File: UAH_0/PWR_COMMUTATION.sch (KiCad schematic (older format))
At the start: 19 parts

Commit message: обновлена схема управления движками
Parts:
- removed R1, R2, R6, R7: Резистор_10_кОм±5%_0,1Вт, MOTOR_RLC:Резистор_SMD_0603-0,075_Вт, symbol MOTOR_2020_import:Резистор_10_кОм±5%_0,1Вт
- removed R3, R4, R5: Резистор_470_Ом±5%_0,1Вт, MOTOR_RLC:Резистор_SMD_0603-0,075_Вт, symbol MOTOR_2020_import:Резистор_470_Ом±5%_0,1Вт
- removed VD3, VD5: Стабилитрон_2С133В, symbol MOTOR_2020_components:Стабилитрон_2С133В
- removed VT1, VT4: MOSFET_P-канал_IRF4905PBF, N_VD_HL:Транзистор_P_IRF9Z24NPBF, symbol elements_2020:MOSFET_P-канал_IRF4905PBF
- added C10, C11, C12, C13, C8, C9: Конденсатор_16В_0.1_мкФ+-10проц., MOTOR_RLC:Конденсатор_SMD_К10-83(0603), symbol MOTOR_2020_import:Конденсатор_16В_0.1_мкФ+-10проц.
- added DD1, DD2: Драйвер_FET-IGBT_IR2103STRPBF, N_DD:SO-8, symbol elements_2020:Драйвер_FET-IGBT_IR2103STRPBF
- added R1, R2: Резистор_CF-100_10_Ом_1Вт, symbol elements:Резистор_1Вт
- added VD1, VD3, VD5, VD7: Диод_шоттки_SK16, N_VD_HL:Диод_SMB, symbol elements_2020:Диод_шоттки_SK16
- added VD6, VD8: Стабилитрон_2С133В, symbol MOTOR_2020_components:Стабилитрон_2С133В
- added VT1, VT4: MOSFET_N-канал_AUIRF3205Z, N_VD_HL:Транзистор_N_STP10NK60Z, symbol elements_2020:MOSFET_N-канал_AUIRF3205Z
- added X4: Check_point, N_X:Пробник, symbol elements_2020:Check_point
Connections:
- net labels added: 15V, GND, MODE_1_H, MODE_1_H_COM, MODE_1_L, MODE_2_H, MODE_2_H_COM, MODE_2_L, VB
- wire segments 78 -> 119
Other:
- moved on the sheet: C5, C6, C7, VD2, VT2, VT3, VT5

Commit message: закончена принципиальная схема, подготовлен мост и обвес на 1й канал
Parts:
- removed C10, C11, C6, C8, C9: Конденсатор_16В_0.1_мкФ+-10проц., MOTOR_RLC:Конденсатор_SMD_К10-83(0603), symbol MOTOR_2020_import:Конденсатор_16В_0.1_мкФ+-10проц.
- removed DD1, DD2: Драйвер_FET-IGBT_IR2103STRPBF, N_DD:SO-8, symbol elements_2020:Драйвер_FET-IGBT_IR2103STRPBF
- removed R1: Резистор_CF-100_10_Ом_1Вт, symbol elements:Резистор_1Вт
- removed VD1, VD3: Диод_шоттки_SK16, N_VD_HL:Диод_SMB, symbol elements_2020:Диод_шоттки_SK16
- removed VD4, VD6, VD8: Стабилитрон_2С133В, symbol MOTOR_2020_components:Стабилитрон_2С133В
- removed VT1, VT2, VT3, VT4, VT5: MOSFET_N-канал_AUIRF3205Z, N_VD_HL:Транзистор_N_STP10NK60Z, symbol elements_2020:MOSFET_N-канал_AUIRF3205Z
- removed X4: Check_point, N_X:Пробник, symbol elements_2020:Check_point
- added C18, C19: Конденсатор_16В_0.1_мкФ+-10проц., MOTOR_RLC:Конденсатор_SMD_К10-83(0603), symbol MOTOR_2020_import:Конденсатор_16В_0.1_мкФ+-10проц.
- added DA1: МОП-реле_КР293КП4_0, N_DD:DIP8, symbol elements:МОП-реле_КР293КП4_0
- added R10, R11: Резистор_Р1-12-0,125-270_Ом±5%-Н-«А», MOTOR_RLC:Резистор_SMD_0805_0,125Вт, symbol MOTOR_2020_components:Резистор_Р1-12-0,125-270_Ом±5%-Н-«А»
- added VD4, VD6: Стабилитрон_1N5352BRLG_вертикальный, N_VD_HL:стабилитрон_DO-201_вертикальный, symbol elements_2020:Стабилитрон_1N5352BRLG_вертикальный
- added VT3, VT4, VT5, VT6: MOSFET_N-канал_STD60N3LH5, N_VD_HL:IGBT_dpak, symbol elements_2020:MOSFET_N-канал_STD60N3LH5
- added X8, X9: Check_point, N_X:Пробник, symbol elements_2020:Check_point
- R12: renamed from R2; footprint (none) -> N_RLC:резистор_C1-4-1_Вт_вертикальный
- renumbered C5 to C20, C12 to C21, C7 to C22, C13 to C23, VD5 to VD3, VD7 to VD5
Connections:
- net labels added: CHANNEL_1, CHANNEL_2, COMMON, GND(12V)
- net labels removed: 0(12V), CONTROL, MODE_1_H, MODE_1_H_COM, MODE_1_L, MODE_2_H, MODE_2_H_COM, MODE_2_L, VB
- wire segments 119 -> 90
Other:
- moved on the sheet: C20, C21, C22, C23, R12, VD2, VD3, VD5

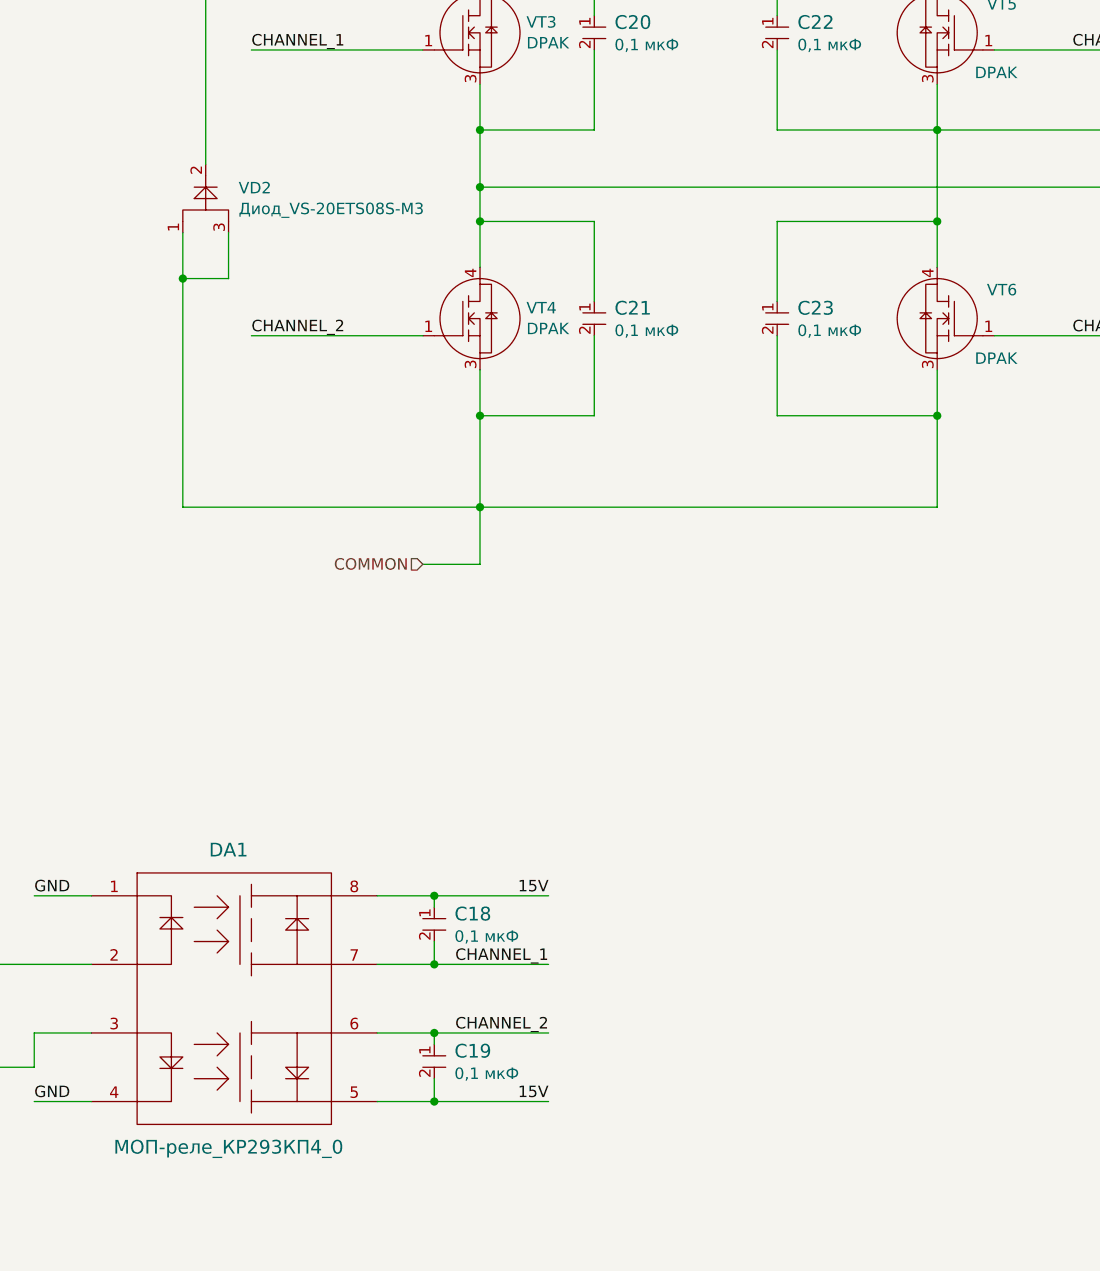
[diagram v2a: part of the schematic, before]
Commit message: расставлена силовая часть на 3 канала, нет управления и главных ключей
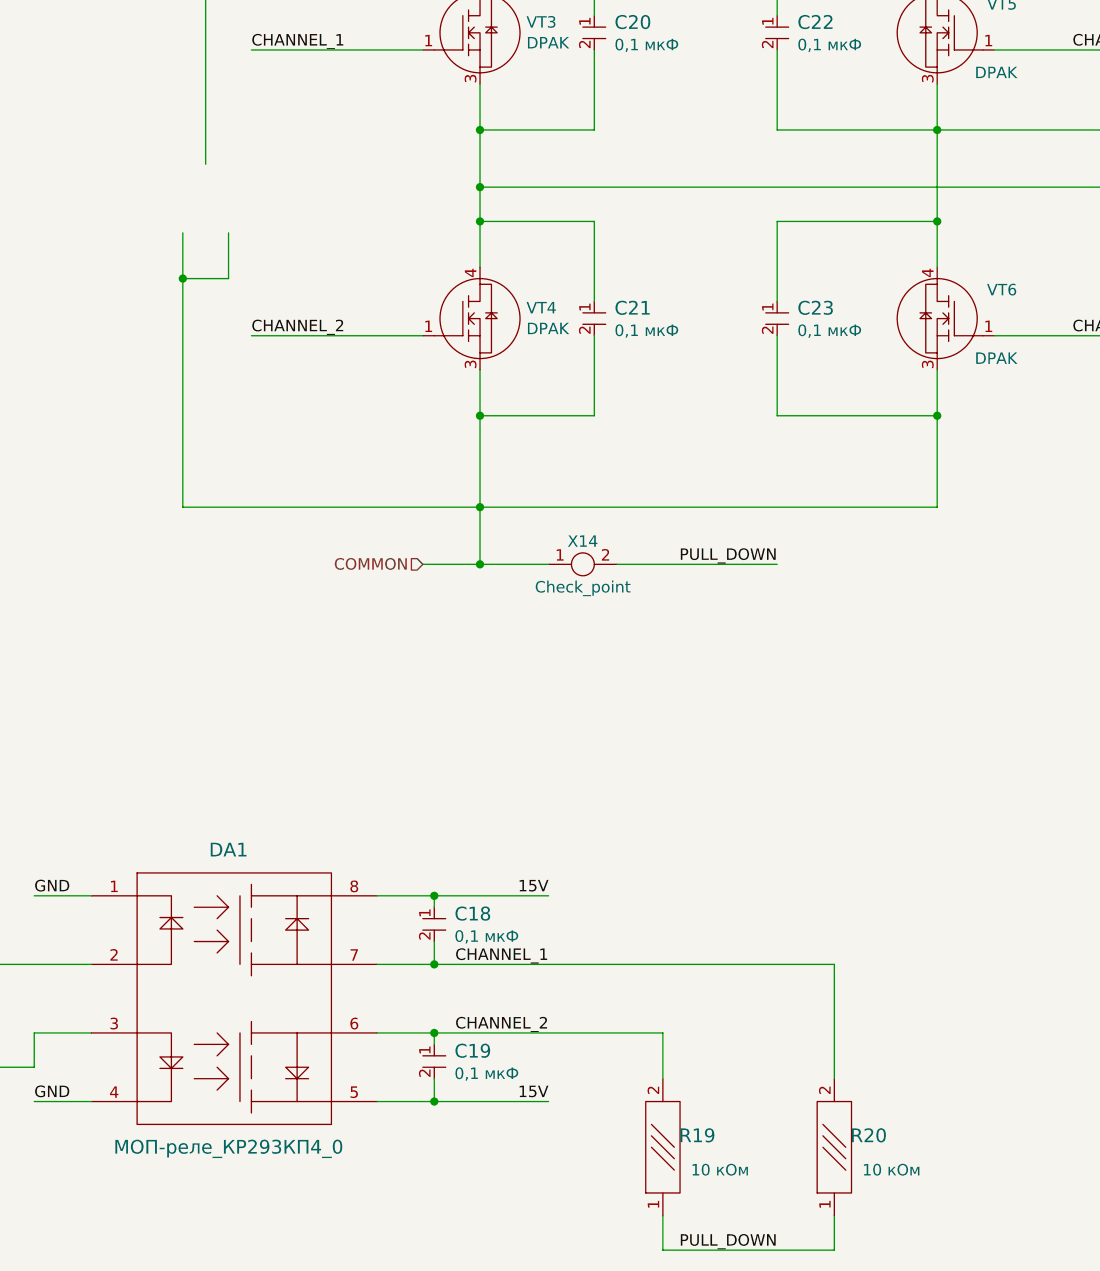
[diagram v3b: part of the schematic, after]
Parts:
- removed VD2: Диод_VS-20ETS08S-M3, N_VD_HL:Транзистор_N-канал_dpak, symbol elements_2020:Диод_VS-20ETS08S-M3
- added R19, R20: Резистор_10_кОм±5%_0,1Вт, MOTOR_RLC:Резистор_SMD_0603-0,075_Вт, symbol MOTOR_2020_import:Резистор_10_кОм±5%_0,1Вт
- added X14: Check_point, N_X:Пробник, symbol elements_2020:Check_point
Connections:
- net labels added: PULL_DOWN
- wire segments 90 -> 97
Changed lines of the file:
@@
 Wire Wire Line
 	6700 3400 6700 3600
-$Comp
-L elements_2020:Диод_VS-20ETS08S-M3 VD2
-U 1 1 5F3CB26D
-P 3400 2800
-AR Path="/5F33B5F7/5F3CB26D" Ref="VD2"  Part="1"
-AR Path="/5F48FE9A/5F3CB26D" Ref="VD7"  Part="1"
-AR Path="/5F495C51/5F3CB26D" Ref="VD12"  Part="1"
-F 0 "VD2" H 3644 2996 50  0000 L CNN
-F 1 "Диод_VS-20ETS08S-M3" H 3644 2905 50  0000 L CNN
-F 2 "N_VD_HL:Транзистор_N-канал_dpak" H 3725 2600 50  0001 C CNN
-F 3 "" V 3400 2700 50  0001 C CNN
-	1    3400 2800
-	1    0    0    -1
-$EndComp
 Wire Wire Line
 	3500 2500 3500 1000
@@
 Wire Wire Line
 	4250 6600 4500 6600
-Wire Wire Line
-	4500 6300 5000 6300
 Connection ~ 4500 6300
-Wire Wire Line
-	4500 6000 5000 6000
 Connection ~ 4500 6000
 Text Label 5000 6000 2    50   ~ 0
@@
 Wire Wire Line
 	8200 2600 8200 4750
+$Comp
+L MOTOR_2020_import:Резистор_10_кОм±5%_0,1Вт R?
+U 1 1 5F3734C7
+P 5500 7100
+AR Path="/5F3734C7" Ref="R?"  Part="1"
+AR Path="/5F33B5F7/5F3734C7" Ref="R19"  Part="1"
+AR Path="/5F48FE9A/5F3734C7" Ref="R21"  Part="1"
+AR Path="/5F495C51/5F3734C7" Ref="R23"  Part="1"
+F 0 "R19" V 5850 6950 60  0000 C CNN
+F 1 "Резистор_10_кОм±5%_0,1Вт" H 5825 6875 60  0001 C CNN
+F 2 "MOTOR_RLC:Резистор_SMD_0603-0,075_Вт" H 5350 6775 60  0001 C CNN
+F 3 "${MOTOR_2020_LIB}\\documentation\\Р1-12_СП.pdf" H 5800 7100 60  0001 C CNN
+F 4 "10 кОм" V 5700 6850 50  0000 C CNN "INFO"
+F 5 "https://www.chipdip.ru/product0/65097" H 5750 7350 50  0001 C CNN "LINK"
+	1    5500 7100
+	0    -1   -1   0
+$EndComp
+$Comp
+L MOTOR_2020_import:Резистор_10_кОм±5%_0,1Вт R?
+U 1 1 5F3761F0
+P 6250 7100
+AR Path="/5F3761F0" Ref="R?"  Part="1"
+AR Path="/5F33B5F7/5F3761F0" Ref="R20"  Part="1"
+AR Path="/5F48FE9A/5F3761F0" Ref="R22"  Part="1"
+AR Path="/5F495C51/5F3761F0" Ref="R24"  Part="1"
+F 0 "R20" V 6600 6950 60  0000 C CNN
+F 1 "Резистор_10_кОм±5%_0,1Вт" H 6575 6875 60  0001 C CNN
+F 2 "MOTOR_RLC:Резистор_SMD_0603-0,075_Вт" H 6100 6775 60  0001 C CNN
+F 3 "${MOTOR_2020_LIB}\\documentation\\Р1-12_СП.pdf" H 6550 7100 60  0001 C CNN
+F 4 "10 кОм" V 6450 6850 50  0000 C CNN "INFO"
+F 5 "https://www.chipdip.ru/product0/65097" H 6500 7350 50  0001 C CNN "LINK"
+	1    6250 7100
+	0    -1   -1   0
+$EndComp
+Wire Wire Line
+	5500 6300 5500 6500
+Wire Wire Line
+	4500 6300 5500 6300
+Wire Wire Line
+	6250 6000 6250 6500
+Wire Wire Line
+	4500 6000 6250 6000
+Wire Wire Line
+	5500 7100 5500 7250
+Wire Wire Line
+	5500 7250 6250 7250
+Wire Wire Line
+	6250 7250 6250 7100
+$Comp
+L elements_2020:Check_point X14
+U 1 1 5F37E3A2
+P 5150 4250
+AR Path="/5F33B5F7/5F37E3A2" Ref="X14"  Part="1"
+AR Path="/5F48FE9A/5F37E3A2" Ref="X15"  Part="1"
+AR Path="/5F495C51/5F37E3A2" Ref="X16"  Part="1"
+F 0 "X14" H 5150 4350 50  0000 C CNN
+F 1 "Check_point" H 5150 4150 50  0000 C CNN
+F 2 "N_X:Пробник" H 5150 4250 50  0001 C CNN
+F 3 "" H 5150 4250 50  0001 C CNN
+	1    5150 4250
+	1    0    0    -1
+$EndComp
+Wire Wire Line
+	5000 4250 4700 4250
+Connection ~ 4700 4250
+Wire Wire Line
+	5300 4250 6000 4250
+Text Label 6000 4250 2    50   ~ 0
+PULL_DOWN
+Text Label 6000 7250 2    50   ~ 0
+PULL_DOWN
 $EndSCHEMATC

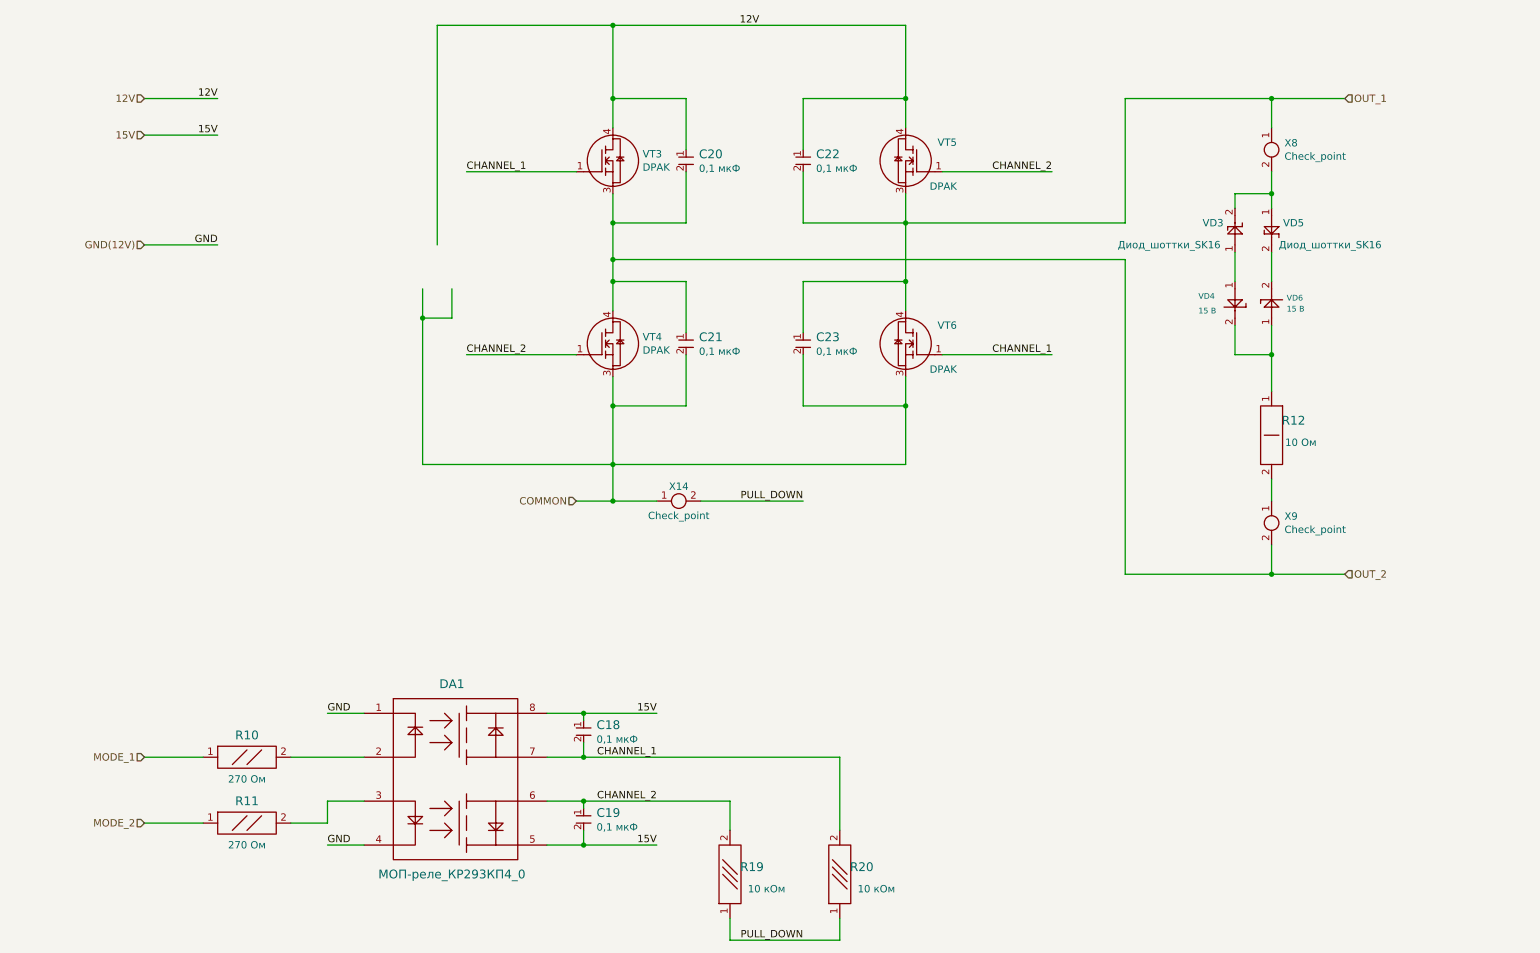
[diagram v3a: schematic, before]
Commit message: не подведены управления DI, габарит определен
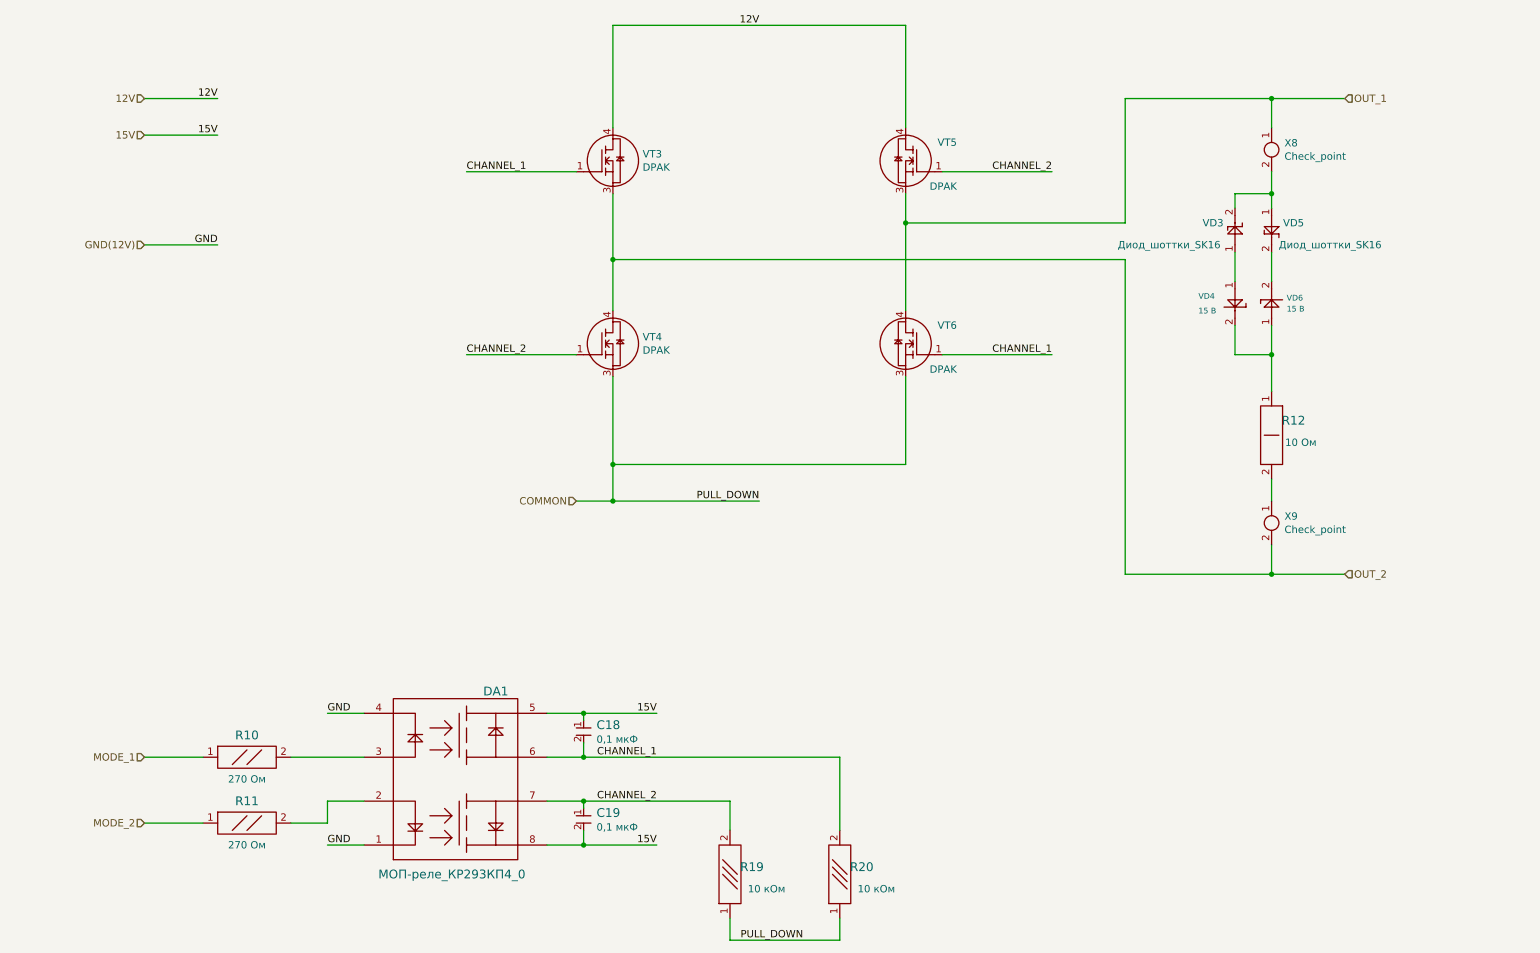
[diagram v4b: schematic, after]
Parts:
- removed C20, C21, C22, C23: Конденсатор_16В_0.1_мкФ+-10проц., MOTOR_RLC:Конденсатор_SMD_К10-83(0603), symbol MOTOR_2020_import:Конденсатор_16В_0.1_мкФ+-10проц.
- removed X14: Check_point, N_X:Пробник, symbol elements_2020:Check_point
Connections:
- wire segments 97 -> 66
